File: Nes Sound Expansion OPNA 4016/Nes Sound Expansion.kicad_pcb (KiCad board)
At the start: 2 copper layers, 86.4 x 87.6 mm, 45 parts, among them J1 NES-SNES Port1, J2 NES-SNES Port2, J3 EXP 1-24, J4 EXP 25-48, J5 EN Switch, J6 AudioJack2_Ground_Switch, J7 EN LED, U1 74LS139, U10 74LS257, U2 74LS132, U6 74LS174, U7 74LS174, U8 74LS257, U9 74LS257, X1 CXO_DIP8

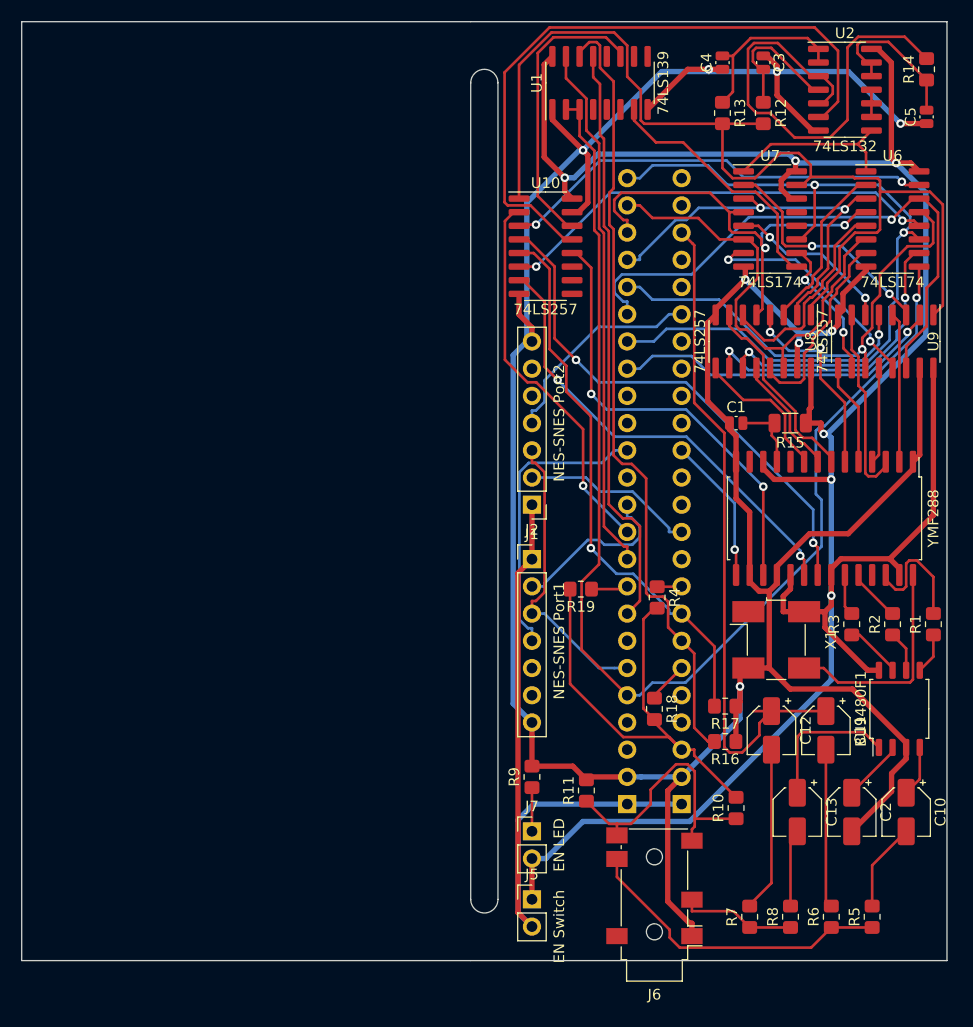
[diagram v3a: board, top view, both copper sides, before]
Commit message: Added logo, 3.5mm 3d module, removed unused stuff
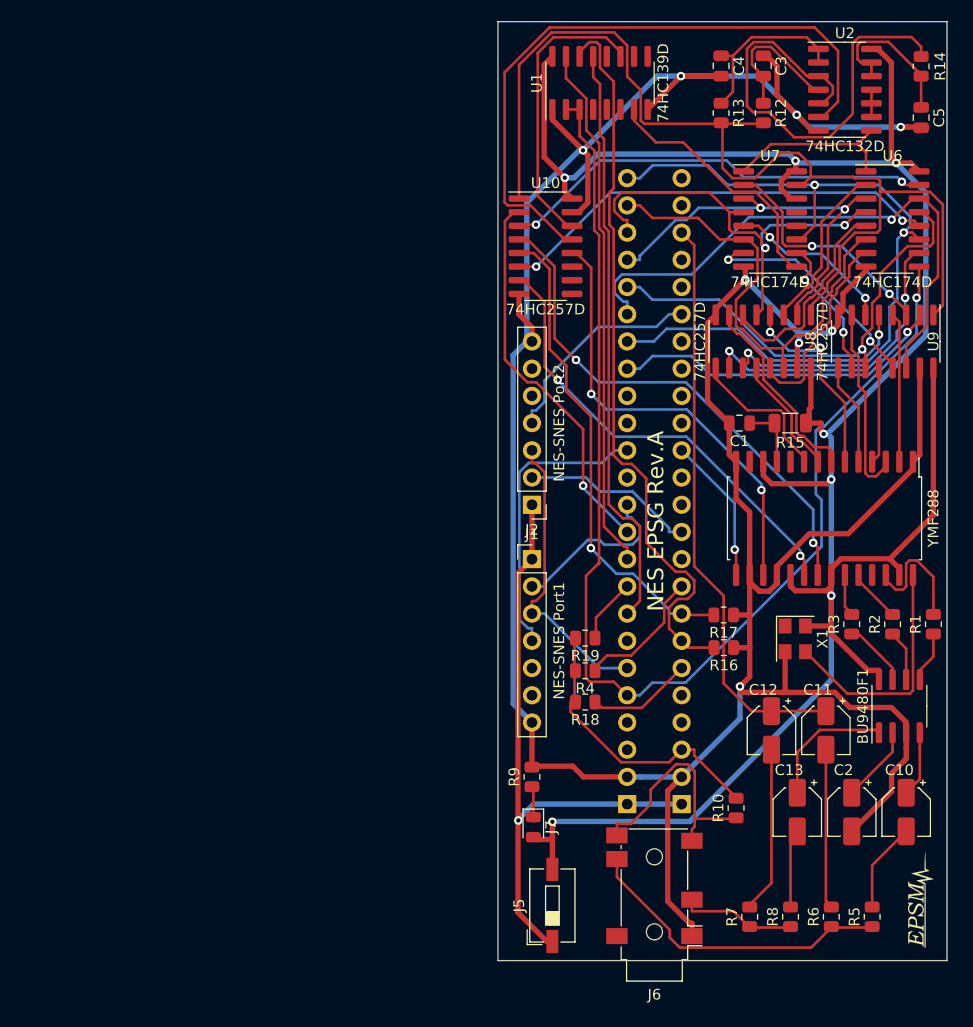
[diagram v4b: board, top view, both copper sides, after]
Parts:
- removed R11: 1k, Resistor_SMD:R_0805_2012Metric_Pad1.20x1.40mm_HandSolder
- added G***: LOGO, Nes Sound Expansion OPNA:EPSM Logo, F.Cu at (135.3, 118.0)
- BU9480F1: footprint Package_SO:SOIC-8_5.275x5.275mm_P1.27mm -> Package_SO:SOIC-8_3.9x4.9mm_P1.27mm
- C1, C3, C4, C5: footprint Capacitor_SMD:C_0504_1310Metric_Pad0.83x1.28mm_HandSolder -> Capacitor_SMD:C_0805_2012Metric
- C10, C11, C12, C13: value 4.7u -> 10uF
- C2: value 10u -> 10uF
- J5: footprint Connector_PinHeader_2.54mm:PinHeader_1x02_P2.54mm_Vertical -> Button_Switch_SMD:SW_DIP_SPSTx01_Slide_6.7x4.1mm_W6.73mm_P2.54mm_LowProfile_JPin
- J7: footprint Connector_PinHeader_2.54mm:PinHeader_1x02_P2.54mm_Vertical -> LED_SMD:LED_0805_2012Metric
- R1, R10, R12, R13, R14, R16, R17, R18, R19, R2, R3, R4, R6, R7, R9: footprint Resistor_SMD:R_0805_2012Metric_Pad1.20x1.40mm_HandSolder -> Resistor_SMD:R_0805_2012Metric
- R5, R8: value 600Ω -> 560; footprint Resistor_SMD:R_0805_2012Metric_Pad1.20x1.40mm_HandSolder -> Resistor_SMD:R_0805_2012Metric
- U1: value 74LS139 -> 74HC139D
- U10, U8, U9: value 74LS257 -> 74HC257D
- U2: value 74LS132 -> 74HC132D
- U6, U7: value 74LS174 -> 74HC174D
- X1: footprint Oscillator:Oscillator_SMD_SeikoEpson_SG8002CA-4Pin_7.0x5.0mm_HandSoldering -> Oscillator:Oscillator_SMD_SeikoEpson_SG8002CE-4Pin_3.2x2.5mm
- moved R4 9.59 mm to (104.0, 96.8), turned to 180 degrees
- moved R16 8.76 mm to (117.0, 94.6)
- moved R17 8.51 mm to (117.0, 91.6)
- moved R18 6.49 mm to (104.0, 99.7), turned to 180 degrees
- moved R19 4.59 mm to (104.0, 93.7)
- moved J5 1.99 mm to (101.0, 118.7), turned to 90 degrees
- moved X1 1.78 mm to (123.6, 93.8)
- moved R14 0.58 mm to (135.4, 40.4)
- moved C5 0.51 mm to (135.4, 45.1), turned to 270 degrees
- moved J7 0.41 mm to (99.2, 111.4), turned to 270 degrees
- moved C4 0.34 mm to (116.7, 40.3), turned to 270 degrees
- moved C3 0.31 mm to (120.7, 40.3)
- moved C1 0.31 mm to (118.4, 73.7), turned to 180 degrees
- moved BU9480F1 0.25 mm to (133.3, 100.1)
- moved R13 0.13 mm to (116.7, 44.7)
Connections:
- C1 pad 1: GND -> Net-(C1-Pad1)
- C1 pad 2: Net-(C1-Pad2) -> GND
- C4 pad 1: GND -> Net-(C4-Pad1)
- C4 pad 2: Net-(C4-Pad2) -> GND
- C5 pad 1: GND -> Net-(C5-Pad1)
- C5 pad 2: Net-(C5-Pad2) -> GND
- J1 pad 5: Net-(J1-Pad5) -> (no net)
- J1 pad 6: Net-(J1-Pad6) -> (no net)
- J2 pad 5: Net-(J2-Pad5) -> (no net)
- J2 pad 6: Net-(J2-Pad6) -> (no net)
- J3 pad 10: Net-(J3-Pad10) -> (no net)
- J3 pad 12: Net-(J3-Pad12) -> (no net)
- J3 pad 13: Net-(J3-Pad13) -> (no net)
- J3 pad 15: Net-(J3-Pad15) -> (no net)
- J3 pad 16: Net-(J3-Pad16) -> (no net)
- J3 pad 17: Net-(J3-Pad17) -> (no net)
- J3 pad 18: Net-(J3-Pad18) -> (no net)
- J3 pad 20: Net-(J3-Pad20) -> (no net)
- J3 pad 21: Net-(J3-Pad21) -> (no net)
- J3 pad 23: Net-(J3-Pad23) -> (no net)
- J3 pad 24: Net-(J3-Pad24) -> (no net)
- J3 pad 4: NMI -> (no net)
- J3 pad 5: Net-(J3-Pad5) -> (no net)
- J4 pad 13: Net-(J4-Pad13) -> (no net)
- J4 pad 15: Net-(J4-Pad15) -> (no net)
- J4 pad 16: Net-(J4-Pad16) -> (no net)
- J4 pad 3: Net-(J4-Pad3) -> (no net)
- J4 pad 4: OUT2 -> (no net)
- J4 pad 7: Net-(J4-Pad7) -> (no net)
- J5 pad 1: +5V -> Net-(J1-Pad1)
- J5 pad 2: Net-(J1-Pad1) -> +5V
- R13 pad 1: Net-(C4-Pad2) -> Net-(C4-Pad1)
- R14 pad 1: Net-(C5-Pad2) -> Net-(C5-Pad1)
- R15 pad 2: Net-(C1-Pad2) -> Net-(C1-Pad1)
- U1 pad 10: Net-(U1-Pad10) -> (no net)
- U1 pad 12: Net-(U1-Pad12) -> (no net)
- U1 pad 4: Net-(U1-Pad4) -> (no net)
- U1 pad 5: Net-(U1-Pad5) -> (no net)
- U1 pad 6: Net-(U1-Pad6) -> (no net)
- U1 pad 9: Net-(U1-Pad9) -> (no net)
- U10 pad 10: Net-(U10-Pad10) -> (no net)
- U10 pad 11: Net-(U10-Pad11) -> (no net)
- U10 pad 9: Net-(U10-Pad9) -> (no net)
- U2 pad 1: Net-(C4-Pad2) -> Net-(C4-Pad1)
- U2 pad 12: Net-(C5-Pad2) -> Net-(C5-Pad1)
- U2 pad 13: Net-(C5-Pad2) -> Net-(C5-Pad1)
- U2 pad 2: Net-(C4-Pad2) -> Net-(C4-Pad1)
- U7 pad 12: Net-(U7-Pad12) -> (no net)
- U7 pad 13: Net-(U7-Pad13) -> (no net)
- X1 pad 1: Net-(X1-Pad1) -> (no net)
- YMF288 pad 10: Net-(YMF288-Pad10) -> (no net)
- YMF288 pad 11: Net-(C1-Pad2) -> Net-(C1-Pad1)
- YMF288 pad 13: Net-(YMF288-Pad13) -> (no net)
- YMF288 pad 25: Net-(YMF288-Pad25) -> (no net)
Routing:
- net AudIn: track 44.2 -> 26.9 mm
- net Net-(C4-Pad1): track 0.00 -> 16.1 mm
- net Net-(C4-Pad2): track 16.1 -> 0.00 mm
- net Net-(C5-Pad2): track 14.6 -> 0.00 mm
- net Net-(C5-Pad1): track 0.00 -> 14.4 mm
- net Net-(J3-Pad9): track 2.55 -> 12.7 mm
- net Aud: track 63.3 -> 54.3 mm
- net Net-(J1-Pad1): track 66.8 -> 58.8 mm, vias 0 -> 1
- net A13: track 52.2 -> 45.3 mm
- net Net-(C1-Pad2): track 6.50 -> 0.00 mm
- net Net-(C1-Pad1): track 0.00 -> 6.02 mm
- net Net-(J3-Pad6): track 3.86 -> 9.76 mm
- net A14: track 74.2 -> 68.8 mm
- net GND: track 302.6 -> 307.1 mm
- net Net-(J6-PadSN): track 25.9 -> 22.2 mm
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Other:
- board size 86.4 x 87.6 mm -> 41.9 x 87.6 mm
- board text added: "+5V GND Aud In /NMI A15 EXP9 EXP8 EXP7 EXP6 EXP5 JP2 /OE JP1 D1 JP1 D3 /IRQ JP2 D2 JP2 D3 JP2 /OE JP2 D4 JP2 D0 JP2 D1 Vid Out Aud Out PSU VDD CIC CLK"
- board text added: "+5V GND NC OUT2 OUT1 OUT0 EXP0 EXP1 EXP2 EXP3 EXP4 JP1 /OE JP1 D4 JP1 D0 JP1 /OE JP1 D2 CPU D0 CPU D1 CPU D2 CPU D3 CPU D4 CPU D5 CPU D6 CPU D7"
- board text added: "EXP8 CE1 (HIgh) EXP3 CE2 (Low) EXP1 CE3 (Low) EXP4 A1 EXP7 A0"
- board text added: "NES EPSG Rev.A"
- board text removed: "NES EPSG Prototype V3"

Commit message: minor updates
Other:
- board text added: "NES EPSM Rev.A"
- board text removed: "NES EPSG Rev.A"
